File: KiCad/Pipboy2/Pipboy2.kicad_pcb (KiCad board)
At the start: 2 copper layers, 46 x 52 mm, 12 parts, among them J1 Battery Socket, J2 LCD Socket, SW1 SW_SPST, SW2 SW_SPST

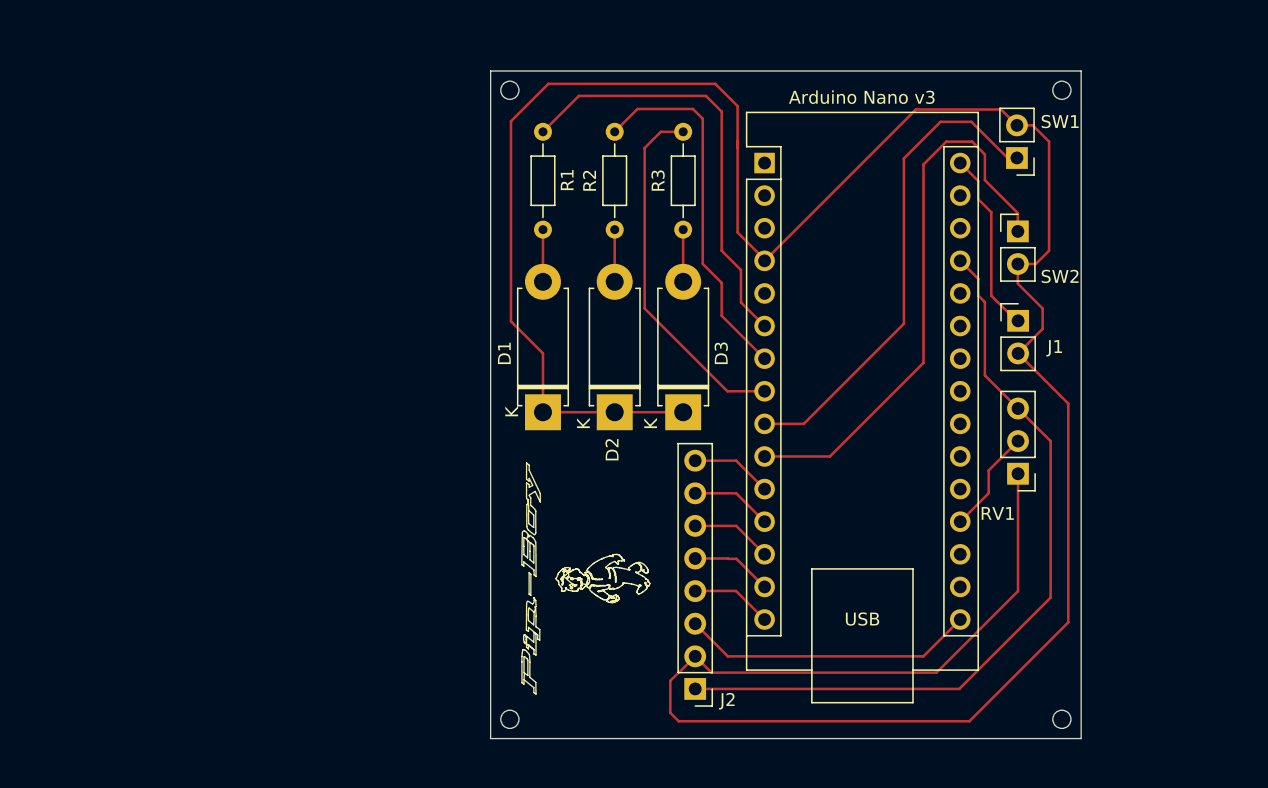
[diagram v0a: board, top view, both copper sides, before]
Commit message: Added voltage reg, power button, updated pcb editor scheme
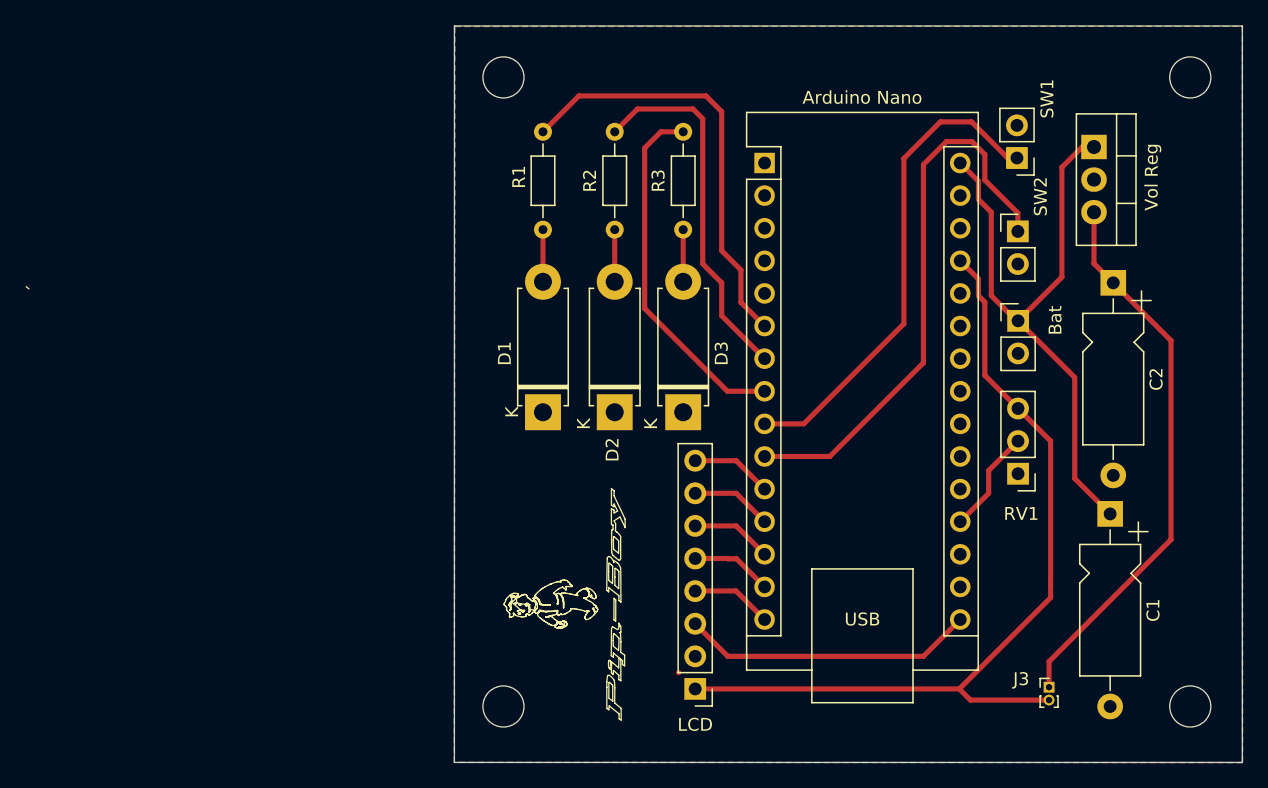
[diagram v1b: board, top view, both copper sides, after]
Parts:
- added C1: 330nF, Capacitor_THT:CP_Axial_L10.0mm_D4.5mm_P15.00mm_Horizontal, F.Cu at (155.3, 106.0)
- added C2: 100nF, Capacitor_THT:CP_Axial_L10.0mm_D4.5mm_P15.00mm_Horizontal, F.Cu at (155.5, 88.0)
- added H1: MountingHole, MountingHole:MountingHole_3.2mm_M3, F.Cu at (161.5, 72.0)
- added H2: MountingHole, MountingHole:MountingHole_3.2mm_M3, F.Cu at (108.0, 72.0)
- added H3: MountingHole, MountingHole:MountingHole_3.2mm_M3, F.Cu at (108.0, 121.0)
- added H4: MountingHole, MountingHole:MountingHole_3.2mm_M3, F.Cu at (161.5, 121.0)
- added J3: Power Button, Connector_PinHeader_1.00mm:PinHeader_1x02_P1.00mm_Vertical, F.Cu at (150.5, 119.5)
- added Vol Reg: L7805, Package_TO_SOT_THT:TO-220-3_Vertical, F.Cu at (154.0, 77.4)
- Arduino Nano: renamed from Arduino Nano v3
- Bat: renamed from J1; value Battery Socket -> Bat
- renumbered J2 to LCD
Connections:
- Arduino Nano pad 30: Net-(A1-VIN) -> unconnected-(A1-VIN-Pad30)
- Bat pad 1: Net-(A1-VIN) -> Net-(J1-Pin_1)
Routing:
- net GND: track 215.3 -> 0.14 mm
- net Net-(J3-Pin_1): track 0.00 -> 43.4 mm
- net Net-(J1-Pin_1): track 0.00 -> 33.7 mm
- net Net-(A1-VIN): track 14.2 -> 0.00 mm
- net (no net): track 0.00 -> 14.2 mm
- net VCC: track 59.8 -> 67.1 mm
- added copper zone on B.Cu, net GND
- added copper zone on F.Cu, net GND
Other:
- board size 46 x 52 mm -> 61.4 x 57.4 mm

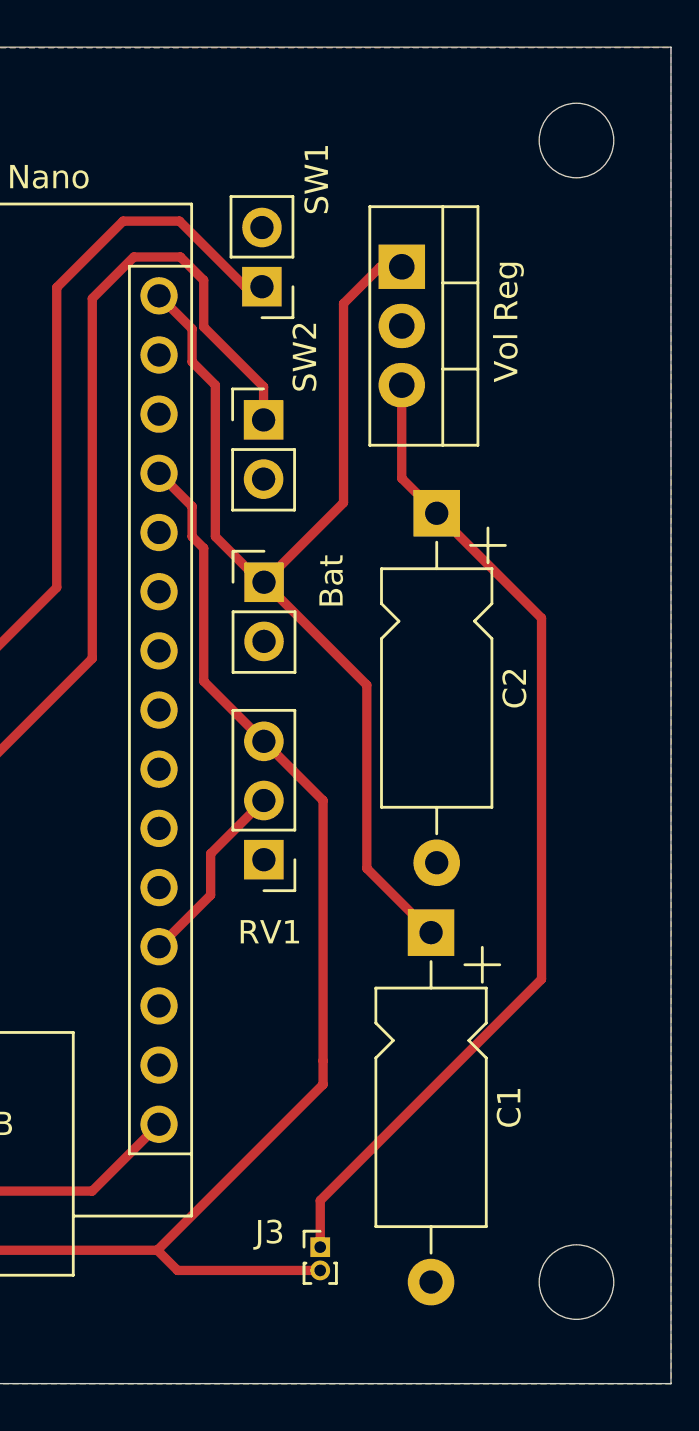
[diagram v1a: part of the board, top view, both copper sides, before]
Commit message: Removed plate violations
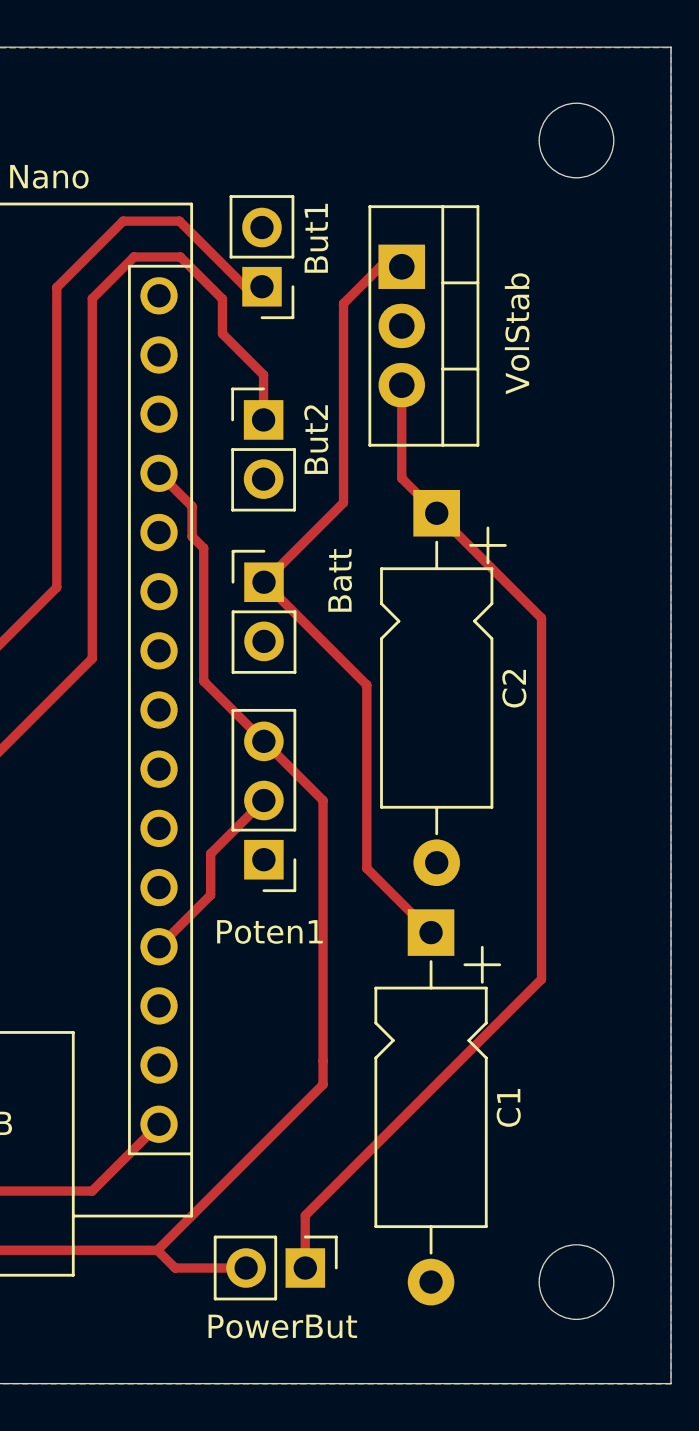
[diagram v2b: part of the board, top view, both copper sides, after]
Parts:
- Batt: renamed from Bat; value Bat -> Battery Socket
- LCD: value LCD Socket -> ~
- PowerBut: renamed from J3; value Power Button -> ~; footprint Connector_PinHeader_1.00mm:PinHeader_1x02_P1.00mm_Vertical -> Connector_PinHeader_2.54mm:PinHeader_1x02_P2.54mm_Vertical
- VolStab: renamed from Vol Reg
- moved PowerBut 1.10 mm to (149.9, 120.4), turned to -90 degrees
- renumbered SW1 to But1, SW2 to But2, RV1 to Poten1
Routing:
- net (no net): track 14.2 -> 0.00 mm
- net VCC: track 67.1 -> 63.9 mm
- net Net-(PowerBut1-Pin_1): track 43.4 -> 44.6 mm
